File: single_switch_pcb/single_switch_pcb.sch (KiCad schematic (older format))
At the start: 6 parts

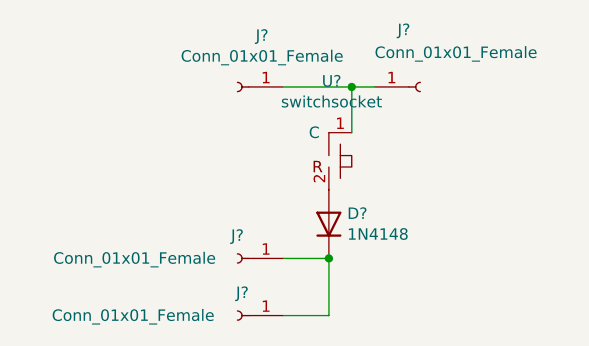
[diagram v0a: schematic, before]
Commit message: created netlist. assigned footprints as well. how about mounting
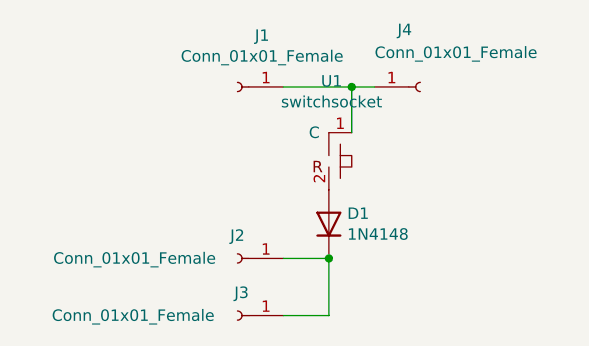
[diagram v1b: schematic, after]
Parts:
- J1, J2, J3, J4: renamed from J?; footprint (none) -> Connector_PinHeader_2.54mm:PinHeader_1x01_P2.54mm_Vertical
- U1: renamed from U?; footprint (none) -> hotswapsocket:hotswap socket
- gave numbers to parts that had none: 1
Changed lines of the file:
@@
 $EndDescr
 $Comp
-L hotswapsocket:switchsocket U?
+L hotswapsocket:switchsocket U1
 U 1 1 620B621F
 P 4850 3000
-F 0 "U?" H 4862 3075 50  0000 C CNN
+F 0 "U1" H 4862 3075 50  0000 C CNN
 F 1 "switchsocket" H 4862 2984 50  0000 C CNN
-F 2 "" H 4850 3000 50  0001 C CNN
+F 2 "hotswapsocket:hotswap socket" H 4850 3000 50  0001 C CNN
 F 3 "" H 4850 3000 50  0001 C CNN
 	1    4850 3000
@@
 $EndComp
 $Comp
-L Diode:1N4148 D?
+L Diode:1N4148 D1
 U 1 1 620B6888
 P 4850 3550
-F 0 "D?" V 4896 3470 50  0000 R CNN
+F 0 "D1" V 4896 3470 50  0000 R CNN
 F 1 "1N4148" V 4805 3470 50  0000 R CNN
 F 2 "Diode_THT:D_DO-35_SOD27_P7.62mm_Horizontal" H 4850 3375 50  0001 C CNN
@@
 $EndComp
 $Comp
-L Connector:Conn_01x01_Female J?
+L Connector:Conn_01x01_Female J3
 U 1 1 620B9287
 P 4450 3950
-F 0 "J?" H 4400 3850 50  0000 L CNN
+F 0 "J3" H 4400 3850 50  0000 L CNN
 F 1 "Conn_01x01_Female" H 4550 3950 50  0000 L CNN
-F 2 "" H 4450 3950 50  0001 C CNN
+F 2 "Connector_PinHeader_2.54mm:PinHeader_1x01_P2.54mm_Vertical" H 4450 3950 50  0001 C CNN
 F 3 "~" H 4450 3950 50  0001 C CNN
 	1    4450 3950
@@
 $EndComp
 $Comp
-L Connector:Conn_01x01_Female J?
+L Connector:Conn_01x01_Female J4
 U 1 1 620B7C20
 P 5250 2950
-F 0 "J?" H 5150 3200 50  0000 L CNN
+F 0 "J4" H 5150 3200 50  0000 L CNN
 F 1 "Conn_01x01_Female" H 5050 3100 50  0000 L CNN
-F 2 "" H 5250 2950 50  0001 C CNN
+F 2 "Connector_PinHeader_2.54mm:PinHeader_1x01_P2.54mm_Vertical" H 5250 2950 50  0001 C CNN
 F 3 "~" H 5250 2950 50  0001 C CNN
 	1    5250 2950
@@
 $EndComp
 $Comp
-L Connector:Conn_01x01_Female J?
+L Connector:Conn_01x01_Female J1
 U 1 1 620B89A8
 P 4450 2950
-F 0 "J?" H 4342 2725 50  0000 C CNN
+F 0 "J1" H 4342 2725 50  0000 C CNN
 F 1 "Conn_01x01_Female" H 4342 2816 50  0000 C CNN
-F 2 "" H 4450 2950 50  0001 C CNN
+F 2 "Connector_PinHeader_2.54mm:PinHeader_1x01_P2.54mm_Vertical" H 4450 2950 50  0001 C CNN
 F 3 "~" H 4450 2950 50  0001 C CNN
 	1    4450 2950
@@
 $EndComp
 $Comp
-L Connector:Conn_01x01_Female J?
+L Connector:Conn_01x01_Female J2
 U 1 1 620B991E
 P 4450 3700
-F 0 "J?" H 4450 3600 50  0000 C CNN
+F 0 "J2" H 4450 3600 50  0000 C CNN
 F 1 "Conn_01x01_Female" H 4900 3700 50  0000 C CNN
-F 2 "" H 4450 3700 50  0001 C CNN
+F 2 "Connector_PinHeader_2.54mm:PinHeader_1x01_P2.54mm_Vertical" H 4450 3700 50  0001 C CNN
 F 3 "~" H 4450 3700 50  0001 C CNN
 	1    4450 3700

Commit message: finished routing. need to put M3 mounting holes on each corner then do checks if design is indeed compatible
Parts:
- D1: footprint Diode_THT:D_DO-35_SOD27_P7.62mm_Horizontal -> Diode_SMD:D_SOD-123
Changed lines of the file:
@@
 F 0 "D1" V 4896 3470 50  0000 R CNN
 F 1 "1N4148" V 4805 3470 50  0000 R CNN
-F 2 "Diode_THT:D_DO-35_SOD27_P7.62mm_Horizontal" H 4850 3375 50  0001 C CNN
+F 2 "Diode_SMD:D_SOD-123" H 4850 3375 50  0001 C CNN
 F 3 "https://assets.nexperia.com/documents/data-sheet/1N4148_1N4448.pdf" H 4850 3550 50  0001 C CNN
 	1    4850 3550
